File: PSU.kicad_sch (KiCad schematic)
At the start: 1 part, among them U3 IRM-01-3.3

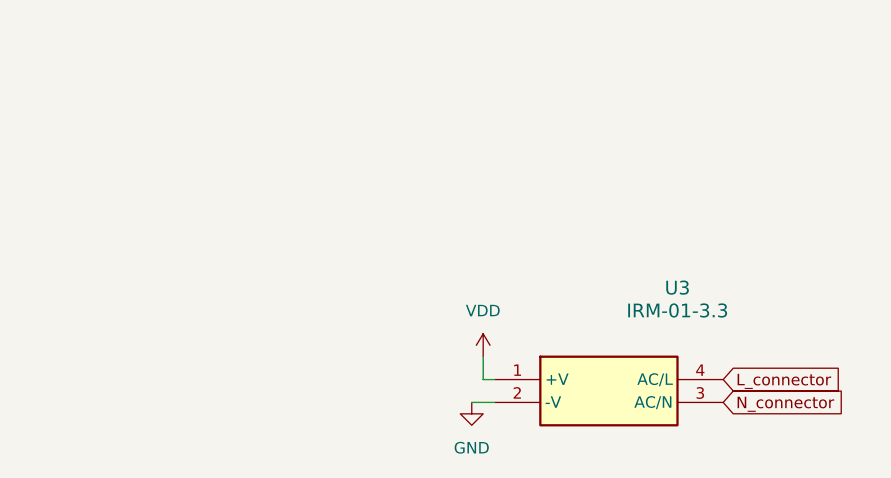
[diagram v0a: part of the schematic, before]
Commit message: poprawka wymiaru płytki
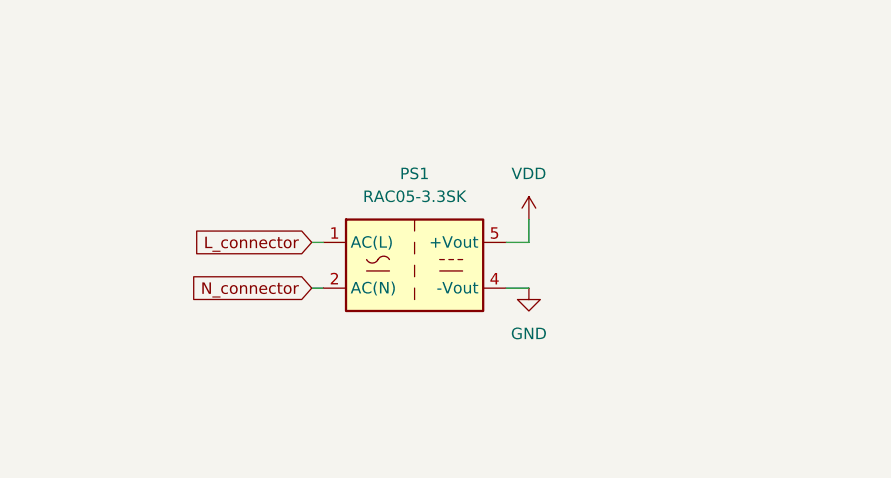
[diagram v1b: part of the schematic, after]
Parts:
- removed U3: IRM-01-3.3, Sterownik_roletyLibrary:IRM015, symbol IRM-01-3_3:IRM-01-3.3
- added PS1: RAC05-3.3SK, Converter_ACDC:Converter_ACDC_RECOM_RAC05-xxSK_THT, symbol Converter_ACDC:RAC05-3.3SK
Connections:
- net GND: now also PS1.4 (-Vout)
- net L_connector: now also PS1.1 (AC(L))
- net N_connector: now also PS1.2 (AC(N))
- net VDD: now also PS1.5 (+Vout)
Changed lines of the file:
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@@
 	(wire
 		(pts
-			(xy 123.19 93.98) (xy 121.92 93.98)
-		)
-		(stroke
-			(width 0)
-			(type default)
-		)
-	)
-	(wire
-		(pts
-			(xy 121.92 93.98) (xy 121.92 91.44)
-		)
-		(stroke
-			(width 0)
-			(type default)
-		)
-	)
-	(wire
-		(pts
-			(xy 120.65 96.52) (xy 123.19 96.52)
+			(xy 102.87 78.74) (xy 104.14 78.74)
+		)
+		(stroke
+			(width 0)
+			(type default)
+		)
+	)
+	(wire
+		(pts
+			(xy 124.46 83.82) (xy 127 83.82)
+		)
+		(stroke
+			(width 0)
+			(type default)
+		)
+	)
+	(wire
+		(pts
+			(xy 127 78.74) (xy 127 76.2)
+		)
+		(stroke
+			(width 0)
+			(type default)
+		)
+	)
+	(wire
+		(pts
+			(xy 124.46 78.74) (xy 127 78.74)
+		)
+		(stroke
+			(width 0)
+			(type default)
+		)
+	)
+	(wire
+		(pts
+			(xy 102.87 83.82) (xy 104.14 83.82)
 		)
 		(stroke
@@
 	(global_label "N_connector"
 		(shape input)
-		(at 148.59 96.52 0)
+		(at 102.87 83.82 180)
 		(fields_autoplaced yes)
 		(effects
@@
 				(size 1.27 1.27)
 			)
-			(justify left)
+			(justify right)
 		)
 		(property "Intersheetrefs" "${INTERSHEET_REFS}"
-			(at 163.247 96.52 0)
-			(effects
-				(font
-					(size 1.27 1.27)
-				)
-				(justify left)
+			(at 88.213 83.82 0)
+			(effects
+				(font
+					(size 1.27 1.27)
+				)
+				(justify right)
 				(hide yes)
 			)
@@
 	(global_label "L_connector"
 		(shape input)
-		(at 148.59 93.98 0)
+		(at 102.87 78.74 180)
 		(fields_autoplaced yes)
 		(effects
@@
 				(size 1.27 1.27)
 			)
-			(justify left)
+			(justify right)
 		)
 		(property "Intersheetrefs" "${INTERSHEET_REFS}"
-			(at 162.9446 93.98 0)
-			(effects
-				(font
-					(size 1.27 1.27)
-				)
-				(justify left)
+			(at 88.5154 78.74 0)
+			(effects
+				(font
+					(size 1.27 1.27)
+				)
+				(justify right)
 				(hide yes)
 			)
@@
 	(symbol
 		(lib_id "power:VDD")
-		(at 121.92 91.44 0)
+		(at 127 76.2 0)
 		(unit 1)
 		(exclude_from_sim no)
@@
 		(dnp no)
 		(fields_autoplaced yes)
-		(property "Reference" "#PWR015"
-			(at 121.92 95.25 0)
+		(property "Reference" "#PWR016"
+			(at 127 80.01 0)
 			(effects
 				(font
@@
 		)
 		(property "Value" "VDD"
-			(at 121.92 86.36 0)
+			(at 127 71.12 0)
 			(effects
 				(font
@@
 		)
 		(property "Footprint" ""
-			(at 121.92 91.44 0)
+			(at 127 76.2 0)
 			(effects
 				(font
@@
 		)
 		(property "Datasheet" ""
-			(at 121.92 91.44 0)
+			(at 127 76.2 0)
 			(effects
 				(font
@@
 		)
 		(property "Description" "Power symbol creates a global label with name \"VDD\""
-			(at 121.92 91.44 0)
+			(at 127 76.2 0)
 			(effects
 				(font
@@
 			(project ""
 				(path "/e63e39d7-6ac0-4ffd-8aa3-1841a4541b55/d9942cb9-a0c0-49db-85f2-749386b323ae"
-					(reference "#PWR015")
+					(reference "#PWR016")
 					(unit 1)
 				)
@@
 	(symbol
 		(lib_id "power:GND")
-		(at 120.65 96.52 0)
+		(at 127 83.82 0)
 		(unit 1)
 		(exclude_from_sim no)
@@
 		(dnp no)
 		(fields_autoplaced yes)
-		(property "Reference" "#PWR014"
-			(at 120.65 102.87 0)
+		(property "Reference" "#PWR017"
+			(at 127 90.17 0)
 			(effects
 				(font
@@
 		)
 		(property "Value" "GND"
-			(at 120.65 101.6 0)
+			(at 127 88.9 0)
 			(effects
 				(font
@@
 		)
 		(property "Footprint" ""
-			(at 120.65 96.52 0)
+			(at 127 83.82 0)
 			(effects
 				(font
@@
 		)
 		(property "Datasheet" ""
-			(at 120.65 96.52 0)
+			(at 127 83.82 0)
 			(effects
 				(font
@@
 		)
 		(property "Description" "Power symbol creates a global label with name \"GND\" , ground"
-			(at 120.65 96.52 0)
+			(at 127 83.82 0)
 			(effects
 				(font
@@
 			(project ""
 				(path "/e63e39d7-6ac0-4ffd-8aa3-1841a4541b55/d9942cb9-a0c0-49db-85f2-749386b323ae"
-					(reference "#PWR014")
+					(reference "#PWR017")
 					(unit 1)
 				)
@@
 	)
 	(symbol
-		(lib_id "IRM-01-3_3:IRM-01-3.3")
-		(at 123.19 93.98 0)
+		(lib_id "Converter_ACDC:RAC05-3.3SK")
+		(at 114.3 81.28 0)
 		(unit 1)
 		(exclude_from_sim no)
@@
 		(dnp no)
 		(fields_autoplaced yes)
-		(property "Reference" "U3"
-			(at 143.51 83.82 0)
-			(effects
-				(font
-					(size 1.524 1.524)
-				)
-			)
-		)
-		(property "Value" "IRM-01-3.3"
-			(at 143.51 86.36 0)
-			(effects
-				(font
-					(size 1.524 1.524)
-				)
-			)
-		)
-		(property "Footprint" "Sterownik_roletyLibrary:IRM015"
-			(at 123.19 93.98 0)
-			(effects
-				(font
-					(size 1.27 1.27)
-					(italic yes)
-				)
-				(hide yes)
-			)
-		)
-		(property "Datasheet" "https://www.meanwell.com/Upload/PDF/IRM-01/IRM-01-SPEC.PDF"
-			(at 123.19 93.98 0)
-			(effects
-				(font
-					(size 1.27 1.27)
-					(italic yes)
-				)
-				(hide yes)
-			)
-		)
-		(property "Description" "Power Supply Encapsulated PCB 3.3V 1W"
-			(at 123.19 93.98 0)
-			(effects
-				(font
-					(size 1.27 1.27)
-				)
-				(hide yes)
-			)
-		)
-		(property "Height" "15"
-			(at 144.78 488.9 0)
-			(effects
-				(font
-					(size 1.27 1.27)
-				)
-				(justify left top)
-				(hide yes)
-			)
-		)
-		(property "Mouser Part Number" "709-IRM01-3.3"
-			(at 144.78 588.9 0)
-			(effects
-				(font
-					(size 1.27 1.27)
-				)
-				(justify left top)
-				(hide yes)
-			)
-		)
-		(property "Mouser Price/Stock" "https://www.mouser.co.uk/ProductDetail/MEAN-WELL/IRM-01-3.3?qs=C9r8PV%2F%252BoWPYMhpLuTFr9w%3D%3D"
-			(at 144.78 688.9 0)
-			(effects
-				(font
-					(size 1.27 1.27)
-				)
-				(justify left top)
-				(hide yes)
-			)
-		)
-		(property "Manufacturer_Name" "Mean Well"
-			(at 144.78 788.9 0)
-			(effects
-				(font
-					(size 1.27 1.27)
-				)
-				(justify left top)
-				(hide yes)
-			)
-		)
-		(property "Manufacturer_Part_Number" "IRM-01-3.3"
-			(at 144.78 888.9 0)
-			(effects
-				(font
-					(size 1.27 1.27)
-				)
-				(justify left top)
-				(hide yes)
-			)
+		(property "Reference" "PS1"
+			(at 114.3 71.12 0)
+			(effects
+				(font
+					(size 1.27 1.27)
+				)
+			)
+		)
+		(property "Value" "RAC05-3.3SK"
+			(at 114.3 73.66 0)
+			(effects
+				(font
+					(size 1.27 1.27)
+				)
+			)
+		)
+		(property "Footprint" "Converter_ACDC:Converter_ACDC_RECOM_RAC05-xxSK_THT"
+			(at 114.3 90.17 0)
+			(effects
+				(font
+					(size 1.27 1.27)
+				)
+				(hide yes)
+			)
+		)
+		(property "Datasheet" "https://www.recom-power.com/pdf/Powerline-AC-DC/RAC05-K.pdf"
+			(at 111.76 73.66 0)
+			(effects
+				(font
+					(size 1.27 1.27)
+				)
+				(hide yes)
+			)
+		)
+		(property "Description" "5W Single Output EMC Class B 3.3V 1515mA"
+			(at 114.3 81.28 0)
+			(effects
+				(font
+					(size 1.27 1.27)
+				)
+				(hide yes)
+			)
+		)
+		(pin "4"
+		)
+		(pin "1"
+		)
+		(pin "3"
+		)
+		(pin "5"
 		)
 		(pin "2"
 		)
-		(pin "3"
-		)
-		(pin "4"
-		)
-		(pin "1"
-		)
 		(instances
-			(project "sterownik_rolety_Zigbee"
+			(project ""
 				(path "/e63e39d7-6ac0-4ffd-8aa3-1841a4541b55/d9942cb9-a0c0-49db-85f2-749386b323ae"
-					(reference "U3")
+					(reference "PS1")
 					(unit 1)
 				)
